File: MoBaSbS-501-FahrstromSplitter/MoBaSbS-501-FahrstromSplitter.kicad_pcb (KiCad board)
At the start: 2 copper layers, 16.5 x 80.6 mm, 7 parts, among them J1 43242-0005, J2 43242-0005, J3 43242-0005, J4 43242-0005, J5 43242-0005

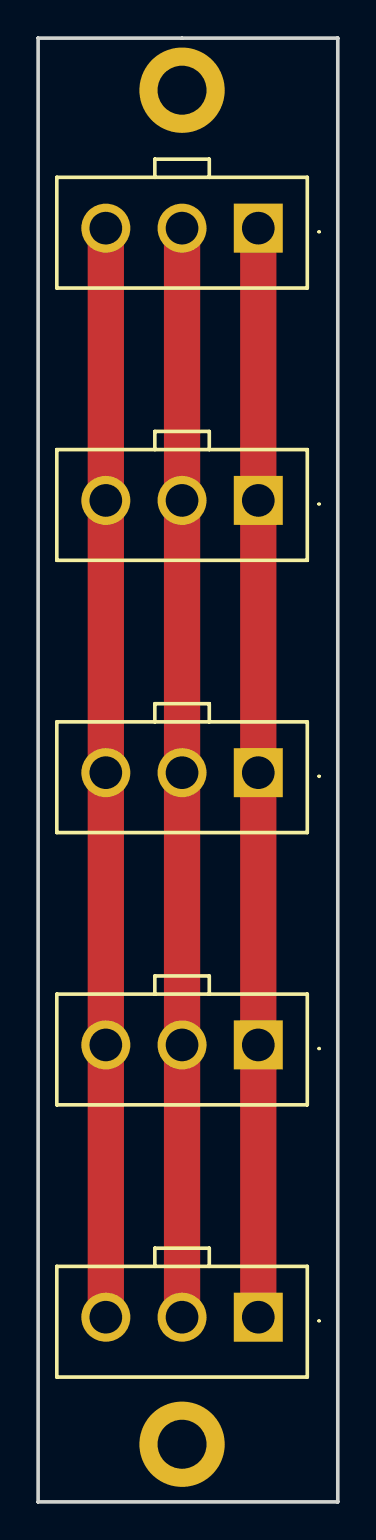
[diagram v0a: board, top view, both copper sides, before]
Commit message: Generated panels, added some new PCBs
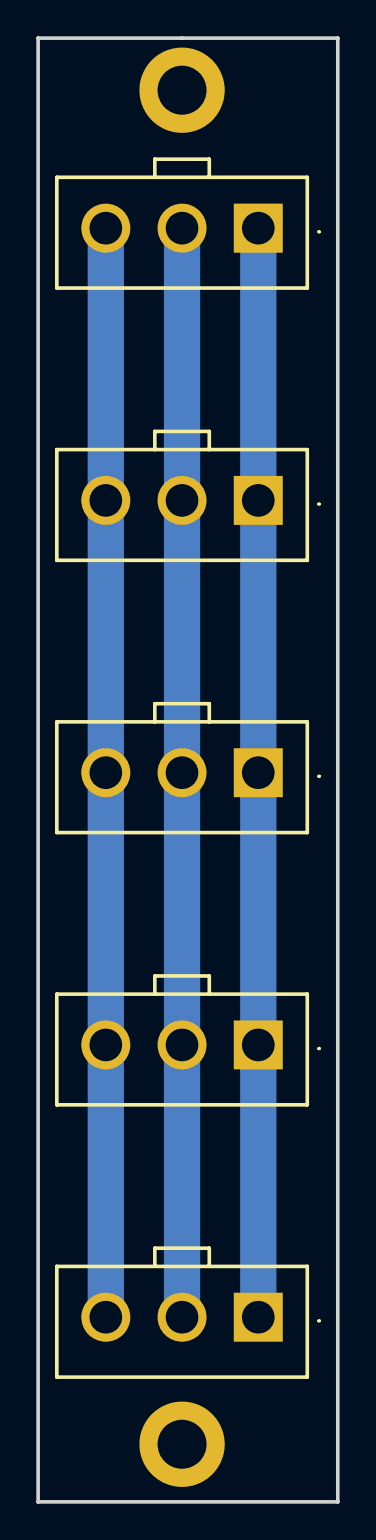
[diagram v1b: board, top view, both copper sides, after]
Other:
- board text added: "MoBaSbs-501/1 10.25 Jomer.dev"
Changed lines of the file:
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@@
 			(psa4output no)
 			(plot_black_and_white yes)
-			(plotinvisibletext no)
 			(sketchpadsonfab no)
 			(plotpadnumbers no)
@@
 		(layer "Edge.Cuts")
 	)
+	(gr_text "MoBaSbs-501/1\n10.25 Jomer.dev"
+		(at 103.251 84.201 0)
+		(layer "B.SilkS")
+		(effects
+			(font
+				(size 1.2 1.2)
+				(thickness 0.3)
+				(bold yes)
+			)
+			(justify right bottom mirror)
+		)
+	)
 	(segment
 		(start 106.6 60)
 		(end 106.6 120)
 		(width 2)
-		(layer "F.Cu")
+		(layer "B.Cu")
 		(net 3)
 	)
@@
 		(end 115 120)
 		(width 2)
-		(layer "F.Cu")
+		(layer "B.Cu")
 		(net 4)
 	)
@@
 		(end 110.8 120)
 		(width 2)
-		(layer "F.Cu")
+		(layer "B.Cu")
 		(net 5)
 	)
